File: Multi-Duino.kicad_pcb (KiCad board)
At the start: 4 copper layers, 68.6 x 53.3 mm, 67 parts, among them J1 M20-9980345, J10 Micro_SD_Card_Det1, J2 M20-9980245, J3 M20-9980345, J4 PPTC101LFBN-RC, J5 PPTC081LFBN-RC, J6 PPTC061LFBN-RC, J7 PPTC081LFBN-RC, J8 USB_C_Receptacle_USB2.0_16P, Q1 FDN340P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

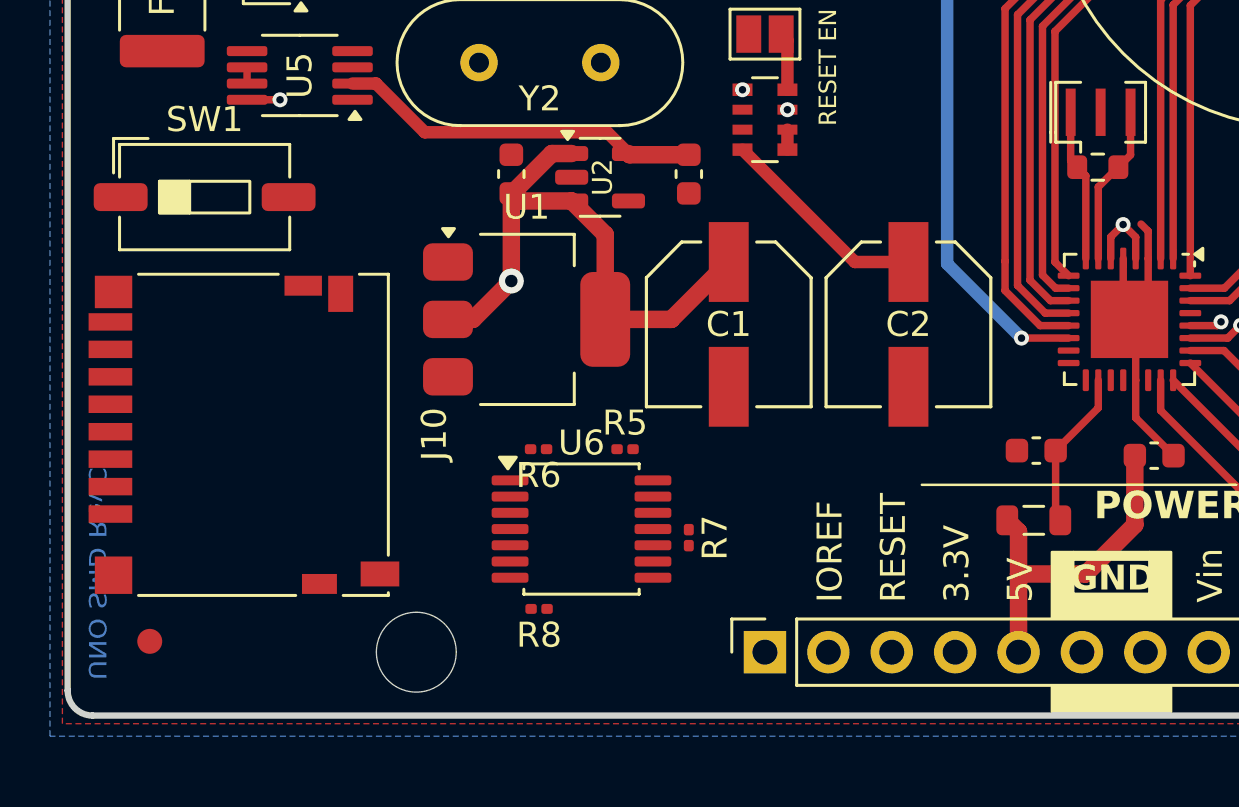
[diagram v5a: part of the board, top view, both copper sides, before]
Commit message: Update Multiduino v2 design
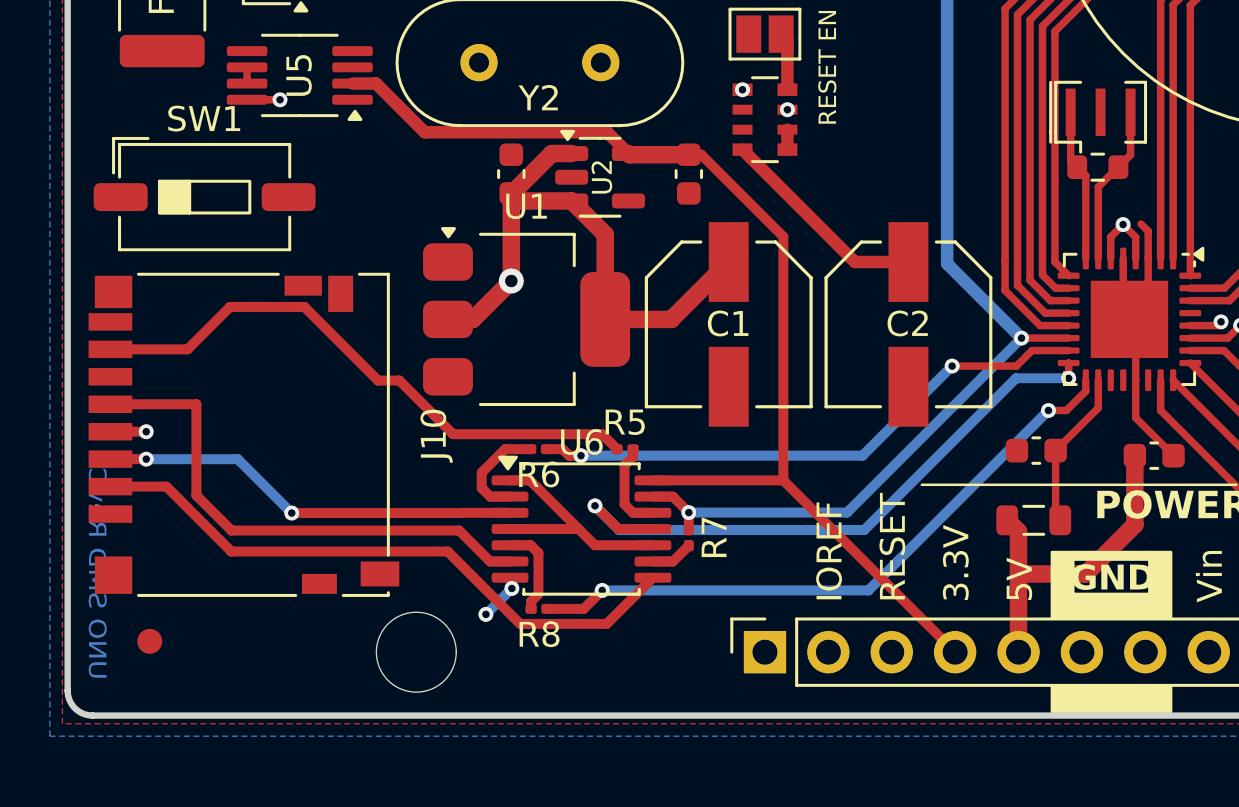
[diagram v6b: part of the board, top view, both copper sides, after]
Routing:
- net +3.3V: track 14.7 -> 46.0 mm, vias 0 -> 1
- net SCK: track 16.0 -> 41.6 mm, vias 0 -> 2
- net MISO: track 0.00 -> 25.2 mm, vias 0 -> 2
- net Net-(J10-DAT3/CD): track 0.00 -> 24.8 mm
- net Net-(J10-DAT0): track 0.00 -> 23.4 mm
- net MOSI: track 16.5 -> 39.3 mm, vias 0 -> 2
- net Net-(J10-CLK): track 0.00 -> 20.8 mm
- net SS: track 30.7 -> 49.4 mm, vias 2 -> 3
- net Net-(J10-CMD): track 0.00 -> 16.9 mm, vias 0 -> 2
- net SW1: track 0.00 -> 9.55 mm
- net Net-(R6-Pad2): track 0.00 -> 4.25 mm
- net Net-(R5-Pad2): track 0.00 -> 3.63 mm
- net Net-(R8-Pad2): track 0.00 -> 3.63 mm
- net Net-(R7-Pad2): track 0.00 -> 1.70 mm
- net GND: track 15.2 -> 16.6 mm, vias 2 -> 4

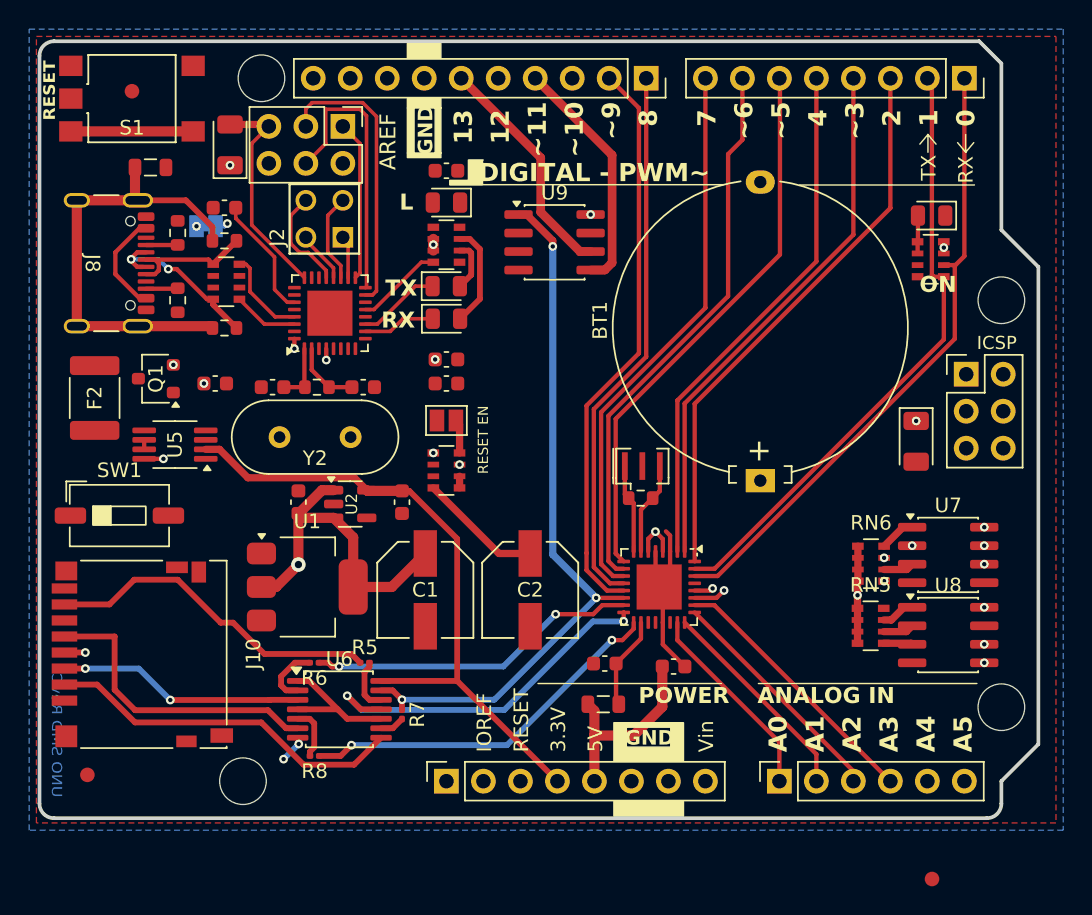
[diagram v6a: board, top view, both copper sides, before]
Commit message: Update Multiduino v2 design
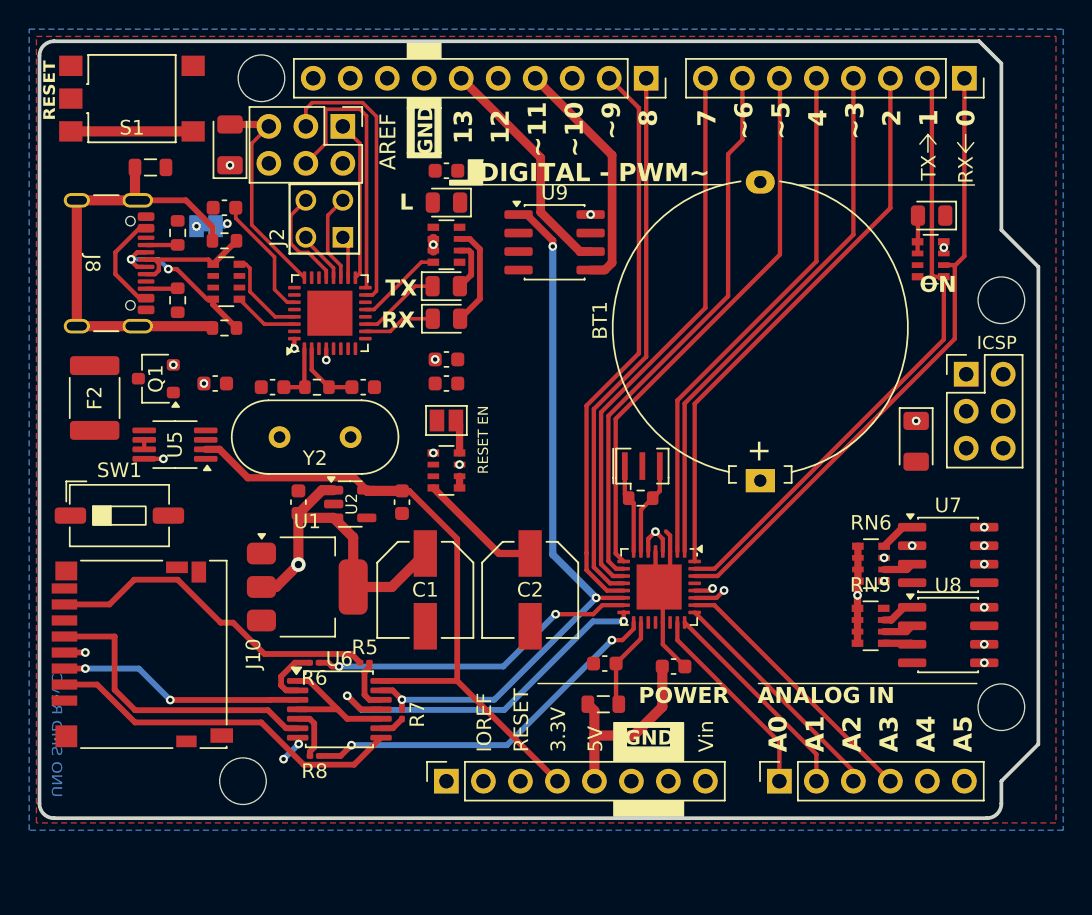
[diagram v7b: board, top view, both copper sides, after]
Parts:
- removed FID1, FID2, FID3: Fiducial, Fiducial:Fiducial_1mm_Mask2mm

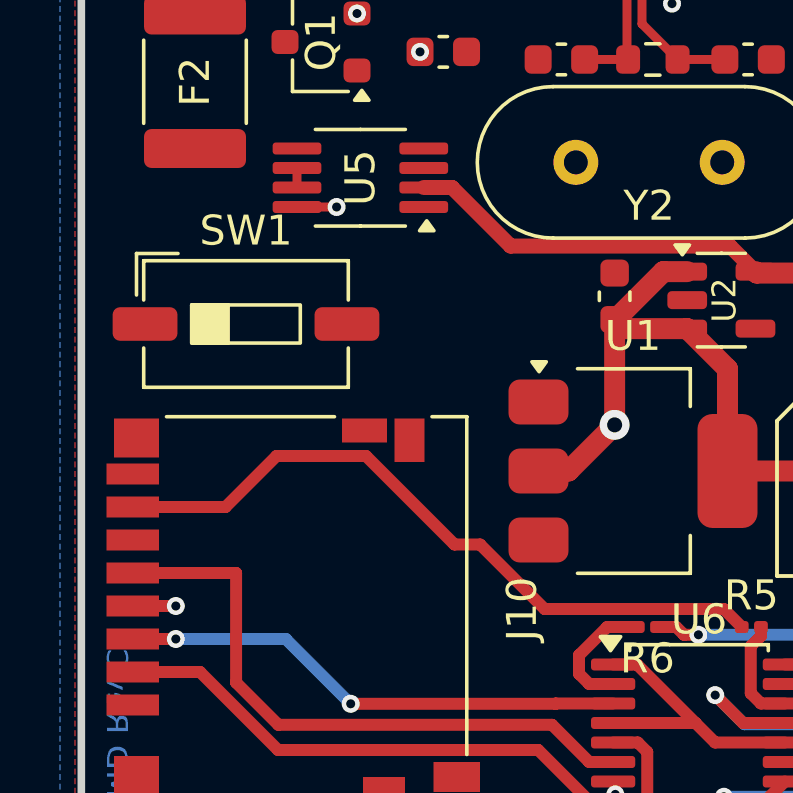
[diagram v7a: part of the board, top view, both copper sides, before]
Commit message: Update Multiduino v2 design
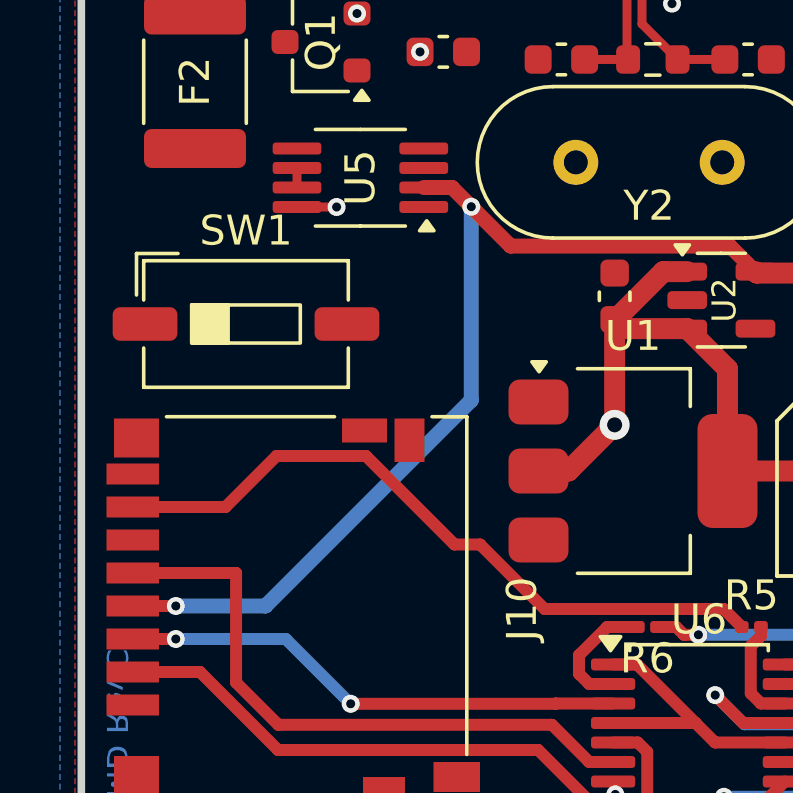
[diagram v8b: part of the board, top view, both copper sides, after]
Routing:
- net +3.3V: track 46.0 -> 65.1 mm, vias 1 -> 2
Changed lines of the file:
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@@
 	(segment
 		(start 126.568088 106.35)
-		(end 128.520088 108.302)
+		(end 127.209044 106.990956)
 		(width 0.5)
 		(layer "F.Cu")
@@
 	)
 	(segment
+		(start 127.209044 106.990956)
+		(end 128.520088 108.302)
+		(width 0.5)
+		(layer "F.Cu")
+		(net 4)
+	)
+	(segment
 		(start 125.625 106.35)
 		(end 126.568088 106.35)
 		(width 0.5)
 		(layer "F.Cu")
+		(net 4)
+	)
+	(via
+		(at 127.209044 106.990956)
+		(size 0.6)
+		(drill 0.3)
+		(layers "F.Cu" "B.Cu")
 		(net 4)
 	)
@@
 		(net 4)
 	)
+	(segment
+		(start 120.35 120.3)
+		(end 117.36 120.3)
+		(width 0.5)
+		(layer "B.Cu")
+		(net 4)
+	)
+	(segment
+		(start 127.209044 113.440956)
+		(end 120.35 120.3)
+		(width 0.5)
+		(layer "B.Cu")
+		(net 4)
+	)
+	(segment
+		(start 127.209044 106.990956)
+		(end 127.209044 113.440956)
+		(width 0.5)
+		(layer "B.Cu")
+		(net 4)
+	)
